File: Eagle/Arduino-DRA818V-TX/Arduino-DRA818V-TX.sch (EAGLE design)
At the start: 23 parts, among them M1 ARDUINO_R3_ICSP, X1 SMA, X2 SMA

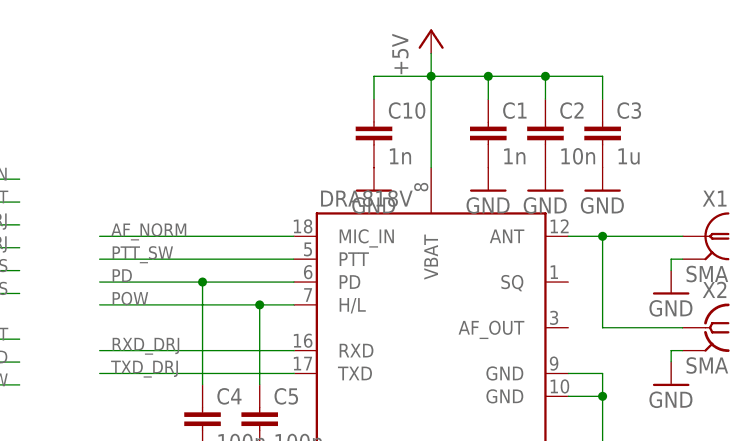
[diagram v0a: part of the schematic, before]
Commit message: Adding Dorji Library
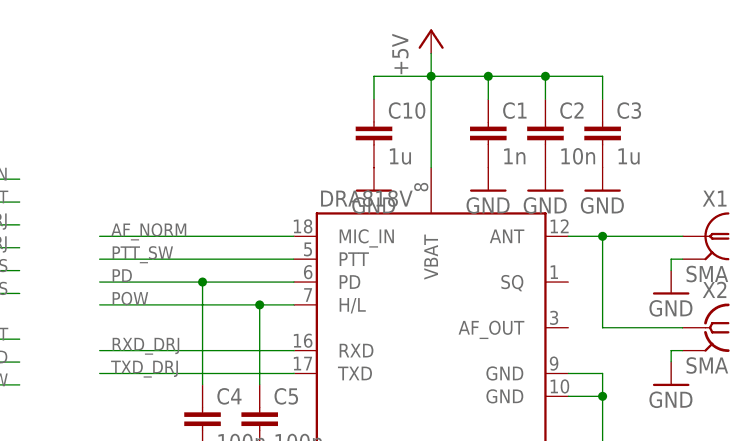
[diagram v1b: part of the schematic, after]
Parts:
- C10: value 1n -> 1u
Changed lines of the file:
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@@
 <part name="GND19" library="supply1" deviceset="GND" device=""/>
 <part name="T1" library="transistor" deviceset="*-NPN-" device="SOT23-BEC" technology="MMBT3904LT1"/>
-<part name="C10" library="resistor" deviceset="C-EU" device="C1206" value="1n"/>
+<part name="C10" library="resistor" deviceset="C-EU" device="C1206" value="1u"/>
 <part name="GND20" library="supply1" deviceset="GND" device=""/>
 <part name="JP1" library="pinhead" deviceset="PINHD-1X4" device=""/>
